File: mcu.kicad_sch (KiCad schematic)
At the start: 9 parts, among them J2 BOOT SEL, SW1 Reset Switch, U2 STM32F030F4Px

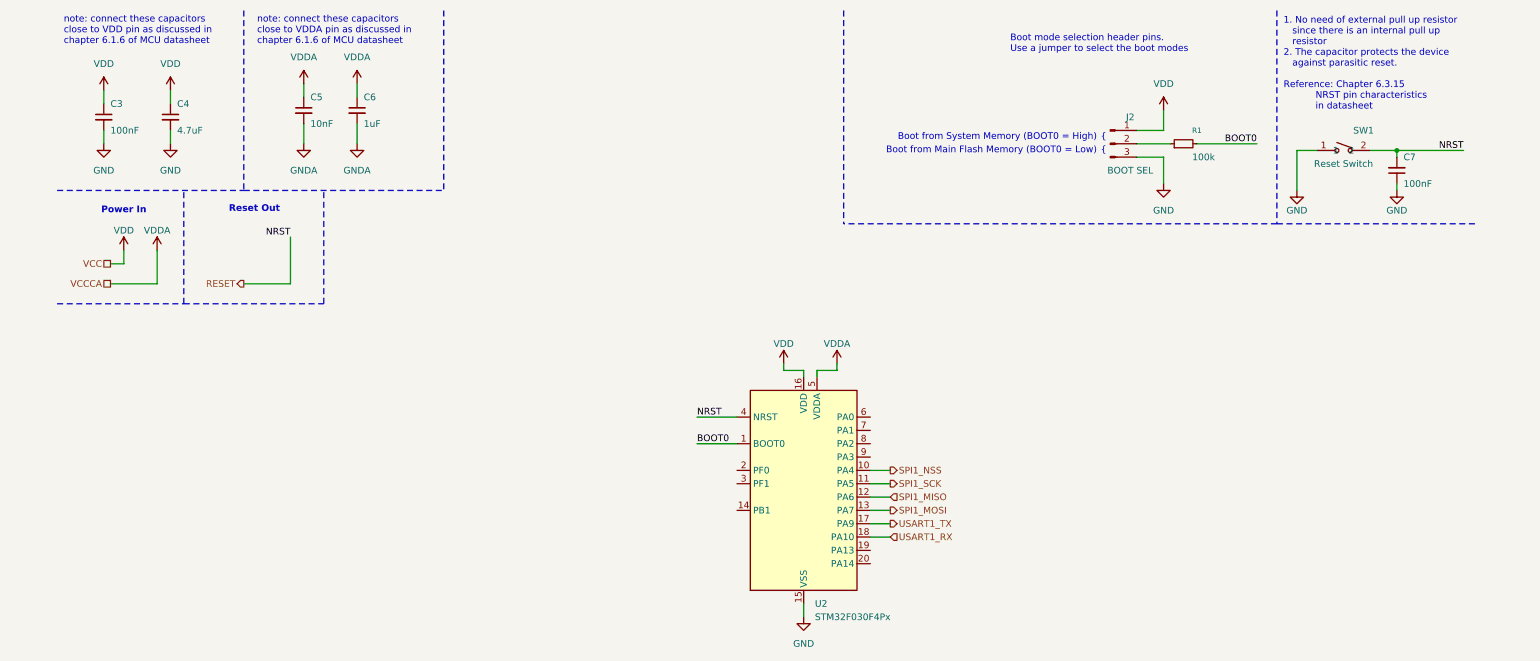
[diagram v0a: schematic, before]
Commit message: fix(erc): "added power and no connect flags to the MCU"
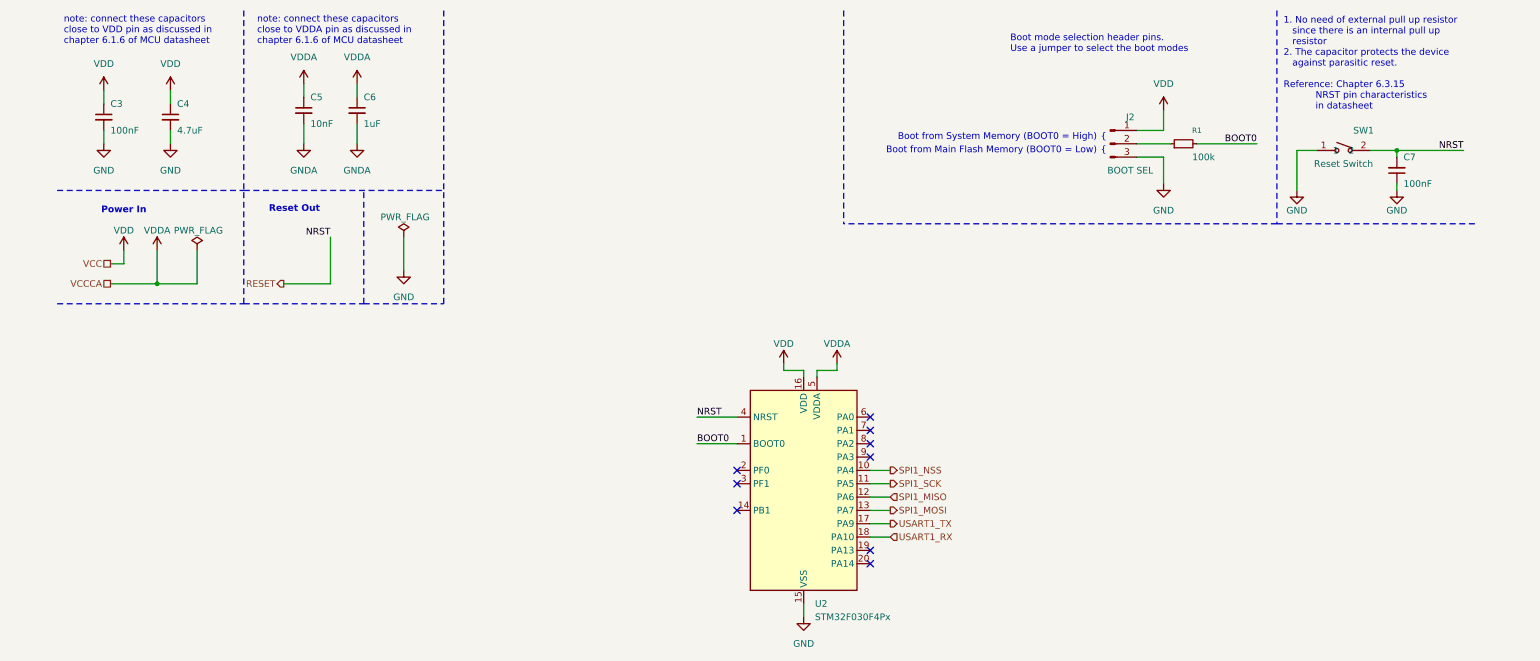
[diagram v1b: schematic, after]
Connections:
- no-connect marks 0 -> 9

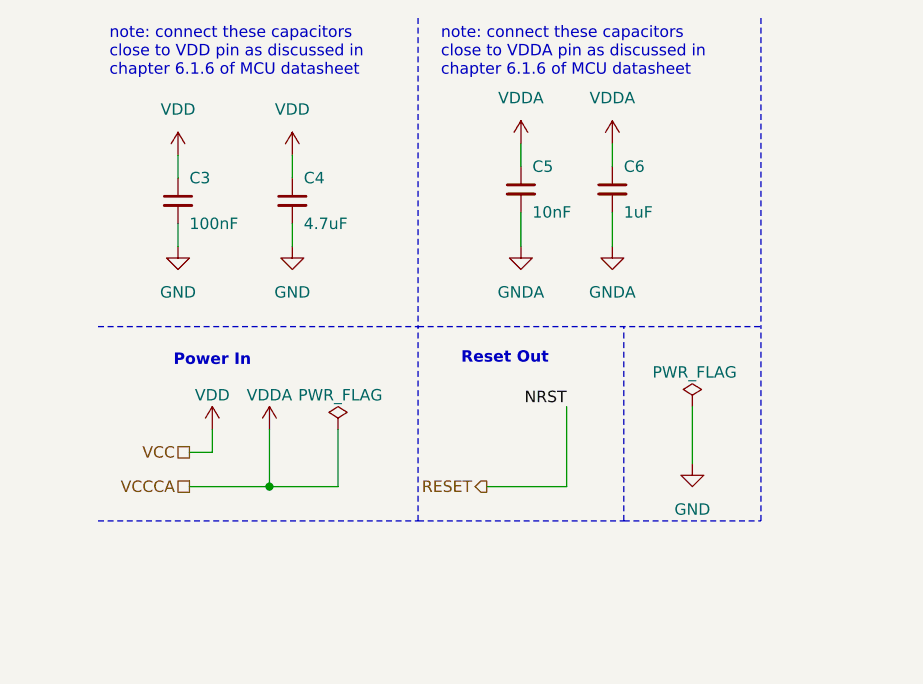
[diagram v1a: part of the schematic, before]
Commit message: fix: moved some power flags to the power tree page
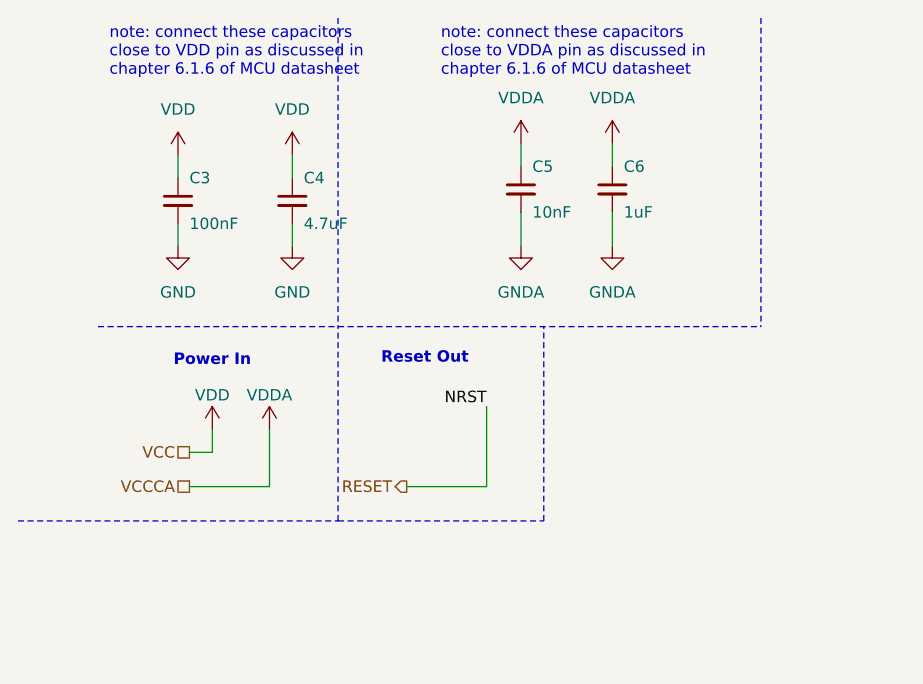
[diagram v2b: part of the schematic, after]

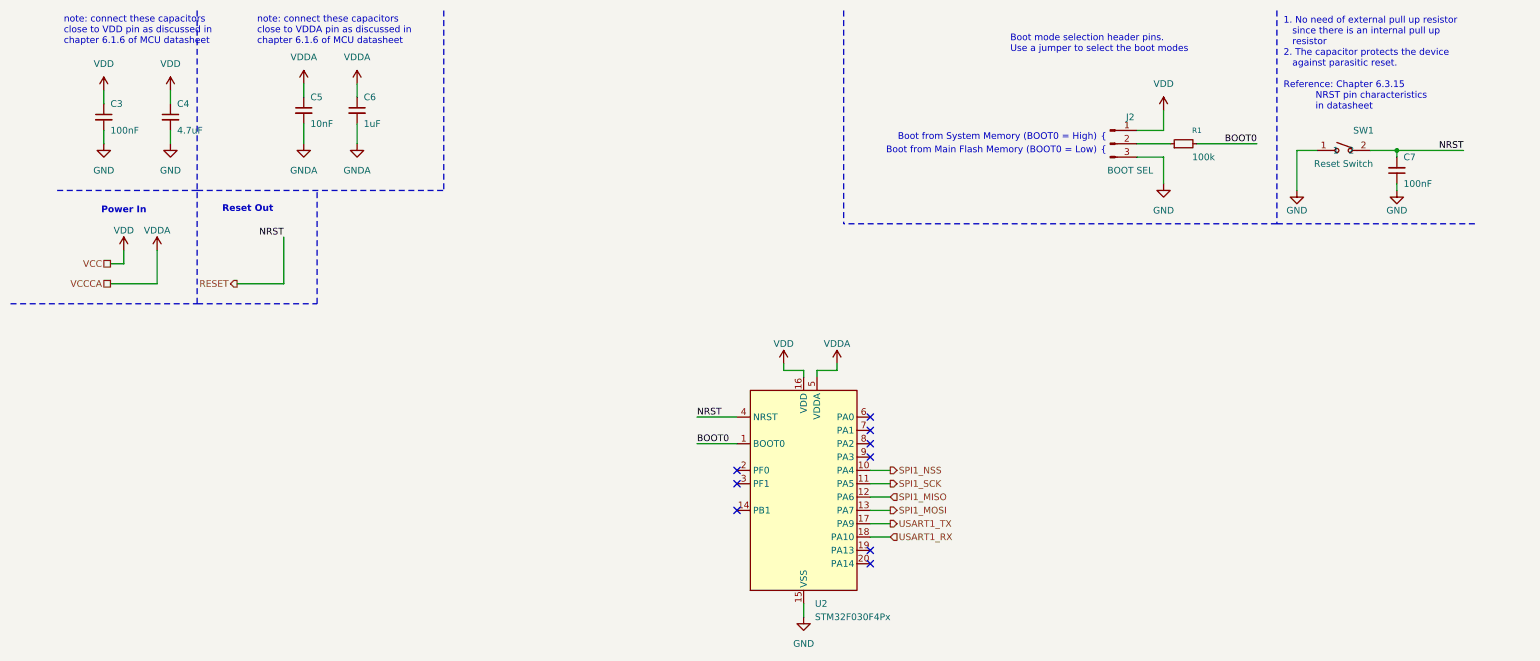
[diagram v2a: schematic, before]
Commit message: refactor(mcu): replace generic VCC/VDD/VDDA with explicit power rails
Replaces generic power:VDD and power:VDDA references with the explicit power:+3.3V and power:+3.3VA rails matching the new power-tree topology. Drops the VCC and VCCCA hierarchical labels (rails are now referenced via power symbols) and reorganizes the power flags and #PWR designators accordingly. Also picks up the KiCad 10 unit-split of TSB008A2530A from the symbol-library migration.
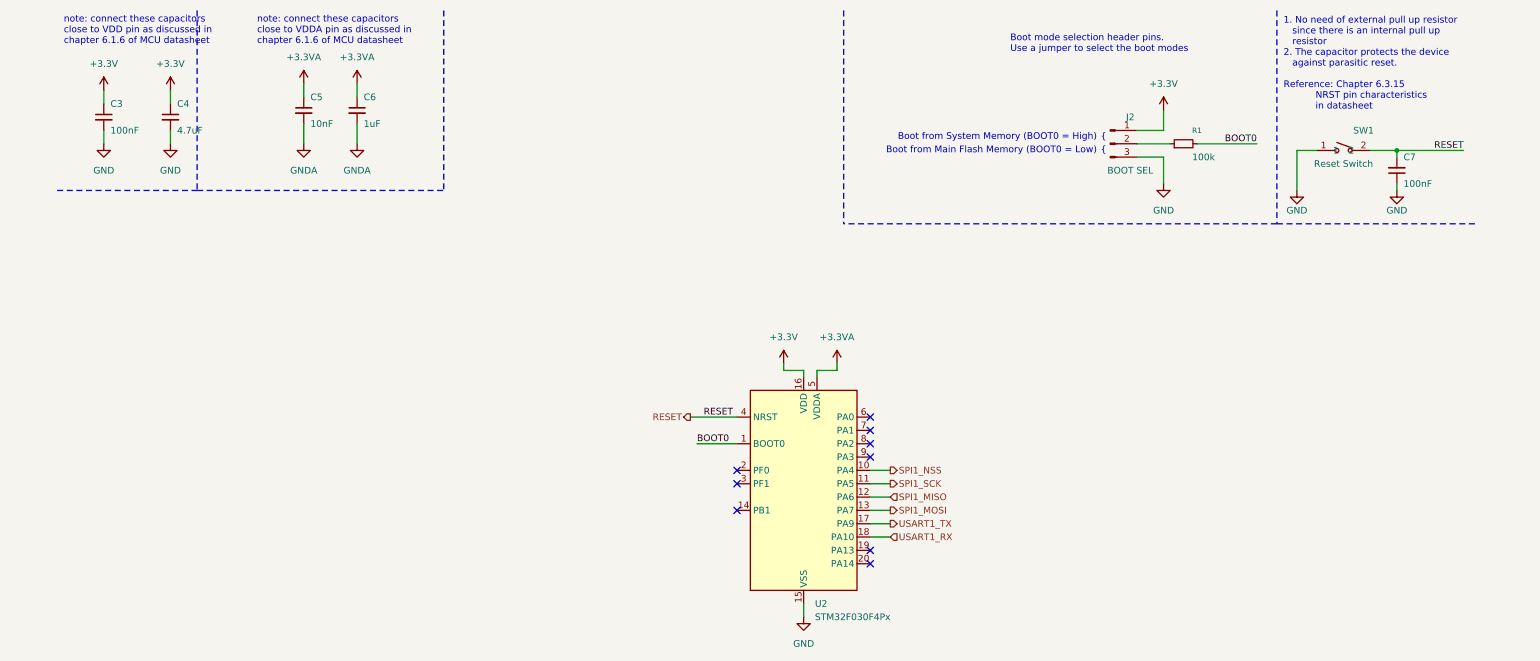
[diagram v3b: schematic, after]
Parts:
- J2: footprint (none) -> Connector_PinHeader_2.54mm:PinHeader_1x02_P2.54mm_Horizontal
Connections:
- net VDD renamed +3.3V
- net VDDA renamed +3.3VA
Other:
- note removed: "Power In"
- note removed: "Reset Out"

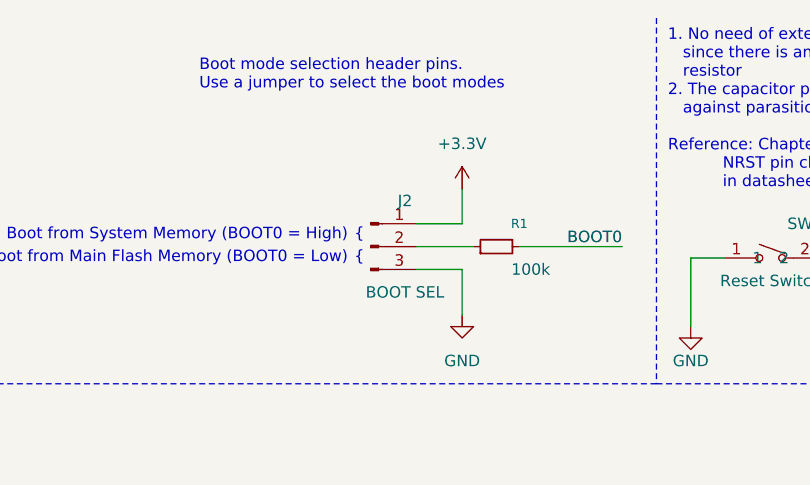
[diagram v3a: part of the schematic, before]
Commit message: fix(fixed_annotation): sorted by x position
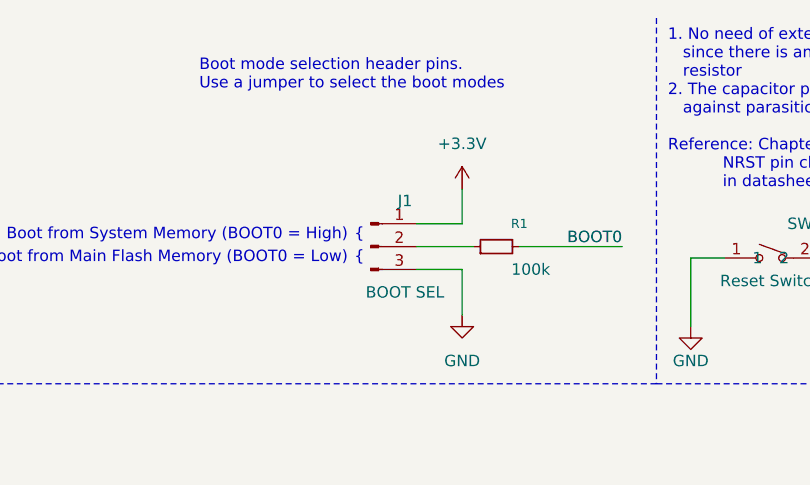
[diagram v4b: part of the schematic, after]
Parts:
- renumbered J2 to J1
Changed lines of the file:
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@@
 		(dnp no)
 		(fields_autoplaced yes)
-		(property "Reference" "#PWR09"
+		(property "Reference" "#PWR011"
 			(at 59.69 30.48 0)
 			(hide yes)
@@
 			(project "HW"
 				(path "/01550cd7-b424-469c-925b-c370f3609cd4/edb1e4c3-83a3-4443-aa4b-0e758d3bea47"
-					(reference "#PWR09")
+					(reference "#PWR011")
 					(unit 1)
 				)
@@
 		(dnp no)
 		(fields_autoplaced yes)
-		(property "Reference" "#PWR010"
+		(property "Reference" "#PWR016"
 			(at 154.94 134.62 0)
 			(hide yes)
@@
 			(project "HW"
 				(path "/01550cd7-b424-469c-925b-c370f3609cd4/edb1e4c3-83a3-4443-aa4b-0e758d3bea47"
-					(reference "#PWR010")
+					(reference "#PWR016")
 					(unit 1)
 				)
@@
 		(dnp no)
 		(fields_autoplaced yes)
-		(property "Reference" "#PWR011"
+		(property "Reference" "#PWR018"
 			(at 223.52 35.56 0)
 			(hide yes)
@@
 			(project "HW"
 				(path "/01550cd7-b424-469c-925b-c370f3609cd4/edb1e4c3-83a3-4443-aa4b-0e758d3bea47"
-					(reference "#PWR011")
+					(reference "#PWR018")
 					(unit 1)
 				)
@@
 		(dnp no)
 		(fields_autoplaced yes)
-		(property "Reference" "#PWR04"
+		(property "Reference" "#PWR07"
 			(at 21.59 31.75 0)
 			(hide yes)
@@
 			(project "HW"
 				(path "/01550cd7-b424-469c-925b-c370f3609cd4/edb1e4c3-83a3-4443-aa4b-0e758d3bea47"
-					(reference "#PWR04")
+					(reference "#PWR07")
 					(unit 1)
 				)
@@
 		(dnp no)
 		(fields_autoplaced yes)
-		(property "Reference" "#PWR06"
+		(property "Reference" "#PWR08"
 			(at 21.59 44.45 0)
 			(hide yes)
@@
 			(project "HW"
 				(path "/01550cd7-b424-469c-925b-c370f3609cd4/edb1e4c3-83a3-4443-aa4b-0e758d3bea47"
-					(reference "#PWR06")
+					(reference "#PWR08")
 					(unit 1)
 				)
@@
 		(dnp no)
 		(fields_autoplaced yes)
-		(property "Reference" "#PWR015"
+		(property "Reference" "#PWR014"
 			(at 69.85 44.45 0)
 			(hide yes)
@@
 			(project "HW"
 				(path "/01550cd7-b424-469c-925b-c370f3609cd4/edb1e4c3-83a3-4443-aa4b-0e758d3bea47"
-					(reference "#PWR015")
+					(reference "#PWR014")
 					(unit 1)
 				)
@@
 		(dnp no)
 		(fields_autoplaced yes)
-		(property "Reference" "#PWR05"
+		(property "Reference" "#PWR09"
 			(at 34.29 31.75 0)
 			(hide yes)
@@
 			(project "HW"
 				(path "/01550cd7-b424-469c-925b-c370f3609cd4/edb1e4c3-83a3-4443-aa4b-0e758d3bea47"
-					(reference "#PWR05")
+					(reference "#PWR09")
 					(unit 1)
 				)
@@
 		(in_pos_files yes)
 		(dnp no)
-		(property "Reference" "J2"
+		(property "Reference" "J1"
 			(at 217.17 33.02 0)
 			(show_name no)
@@
 			(project "HW"
 				(path "/01550cd7-b424-469c-925b-c370f3609cd4/edb1e4c3-83a3-4443-aa4b-0e758d3bea47"
-					(reference "J2")
+					(reference "J1")
 					(unit 1)
 				)
@@
 		(dnp no)
 		(fields_autoplaced yes)
-		(property "Reference" "#PWR040"
+		(property "Reference" "#PWR017"
 			(at 161.29 83.82 0)
 			(hide yes)
@@
 			(project "HW"
 				(path "/01550cd7-b424-469c-925b-c370f3609cd4/edb1e4c3-83a3-4443-aa4b-0e758d3bea47"
-					(reference "#PWR040")
+					(reference "#PWR017")
 					(unit 1)
 				)
@@
 		(dnp no)
 		(fields_autoplaced yes)
-		(property "Reference" "#PWR016"
+		(property "Reference" "#PWR013"
 			(at 69.85 30.48 0)
 			(hide yes)
@@
 			(project "HW"
 				(path "/01550cd7-b424-469c-925b-c370f3609cd4/edb1e4c3-83a3-4443-aa4b-0e758d3bea47"
-					(reference "#PWR016")
+					(reference "#PWR013")
 					(unit 1)
 				)
@@
 		(dnp no)
 		(fields_autoplaced yes)
-		(property "Reference" "#PWR014"
+		(property "Reference" "#PWR012"
 			(at 59.69 44.45 0)
 			(hide yes)
@@
 			(project "HW"
 				(path "/01550cd7-b424-469c-925b-c370f3609cd4/edb1e4c3-83a3-4443-aa4b-0e758d3bea47"
-					(reference "#PWR014")
+					(reference "#PWR012")
 					(unit 1)
 				)
@@
 		(dnp no)
 		(fields_autoplaced yes)
-		(property "Reference" "#PWR07"
+		(property "Reference" "#PWR010"
 			(at 34.29 44.45 0)
 			(hide yes)
@@
 			(project "HW"
 				(path "/01550cd7-b424-469c-925b-c370f3609cd4/edb1e4c3-83a3-4443-aa4b-0e758d3bea47"
-					(reference "#PWR07")
+					(reference "#PWR010")
 					(unit 1)
 				)
@@
 		(dnp no)
 		(fields_autoplaced yes)
-		(property "Reference" "#PWR039"
+		(property "Reference" "#PWR015"
 			(at 151.13 83.82 0)
 			(hide yes)
@@
 			(project "HW"
 				(path "/01550cd7-b424-469c-925b-c370f3609cd4/edb1e4c3-83a3-4443-aa4b-0e758d3bea47"
-					(reference "#PWR039")
+					(reference "#PWR015")
 					(unit 1)
 				)
@@
 		(dnp no)
 		(fields_autoplaced yes)
-		(property "Reference" "#PWR021"
+		(property "Reference" "#PWR019"
 			(at 223.52 52.07 0)
 			(hide yes)
@@
 			(project "HW"
 				(path "/01550cd7-b424-469c-925b-c370f3609cd4/edb1e4c3-83a3-4443-aa4b-0e758d3bea47"
-					(reference "#PWR021")
+					(reference "#PWR019")
 					(unit 1)
 				)
@@
 		(in_pos_files yes)
 		(dnp no)
-		(property "Reference" "#PWR019"
+		(property "Reference" "#PWR021"
 			(at 267.97 53.34 0)
 			(hide yes)
@@
 			(project "HW"
 				(path "/01550cd7-b424-469c-925b-c370f3609cd4/edb1e4c3-83a3-4443-aa4b-0e758d3bea47"
-					(reference "#PWR019")
-					(unit 1)
-				)
+					(reference "#PWR021")
+					(unit 1)
+				)
